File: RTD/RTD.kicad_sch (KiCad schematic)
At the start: 48 parts, among them SW1 SW_SPDT, U1 THVD1420D, U2 STM32F103C8Tx

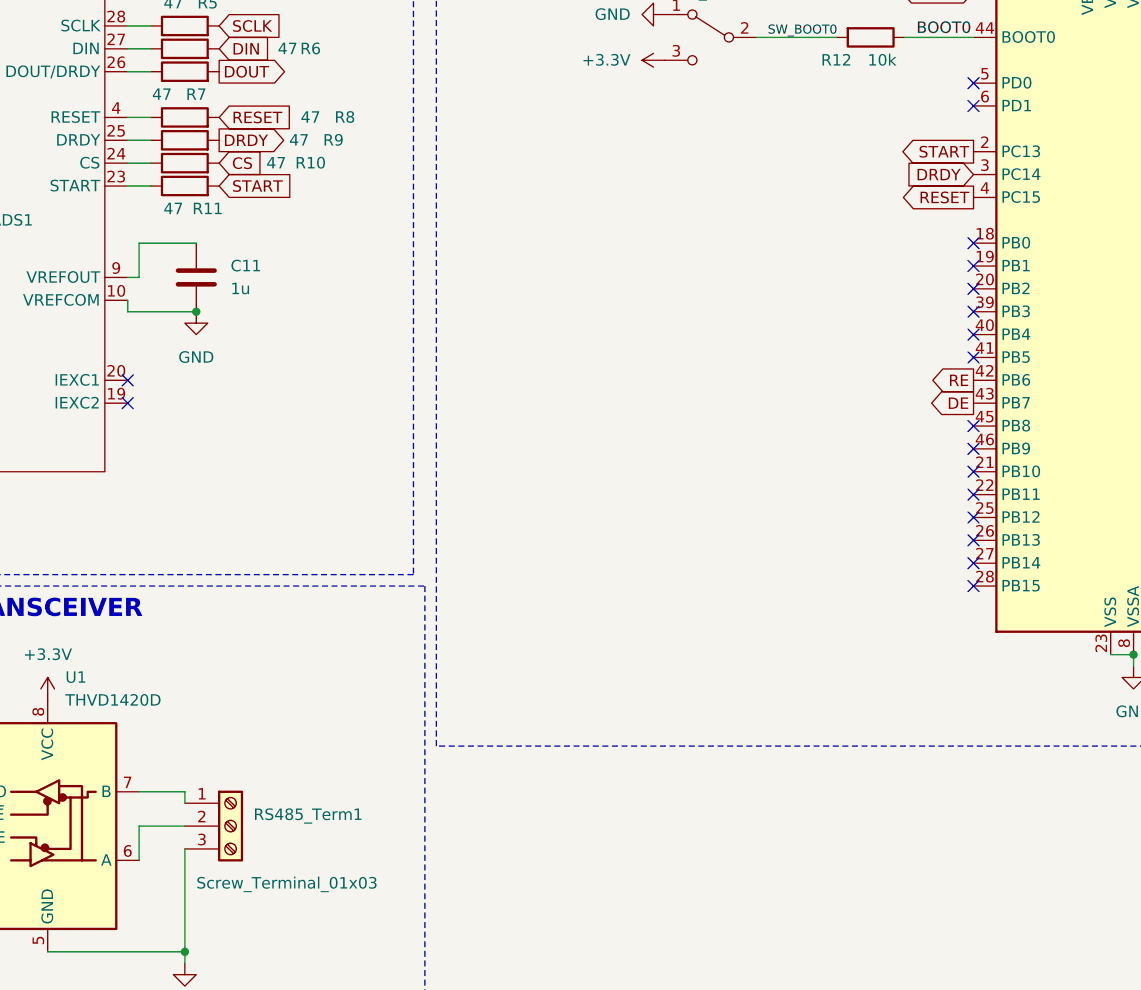
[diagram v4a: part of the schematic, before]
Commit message: feat: adds ADS1248 driver
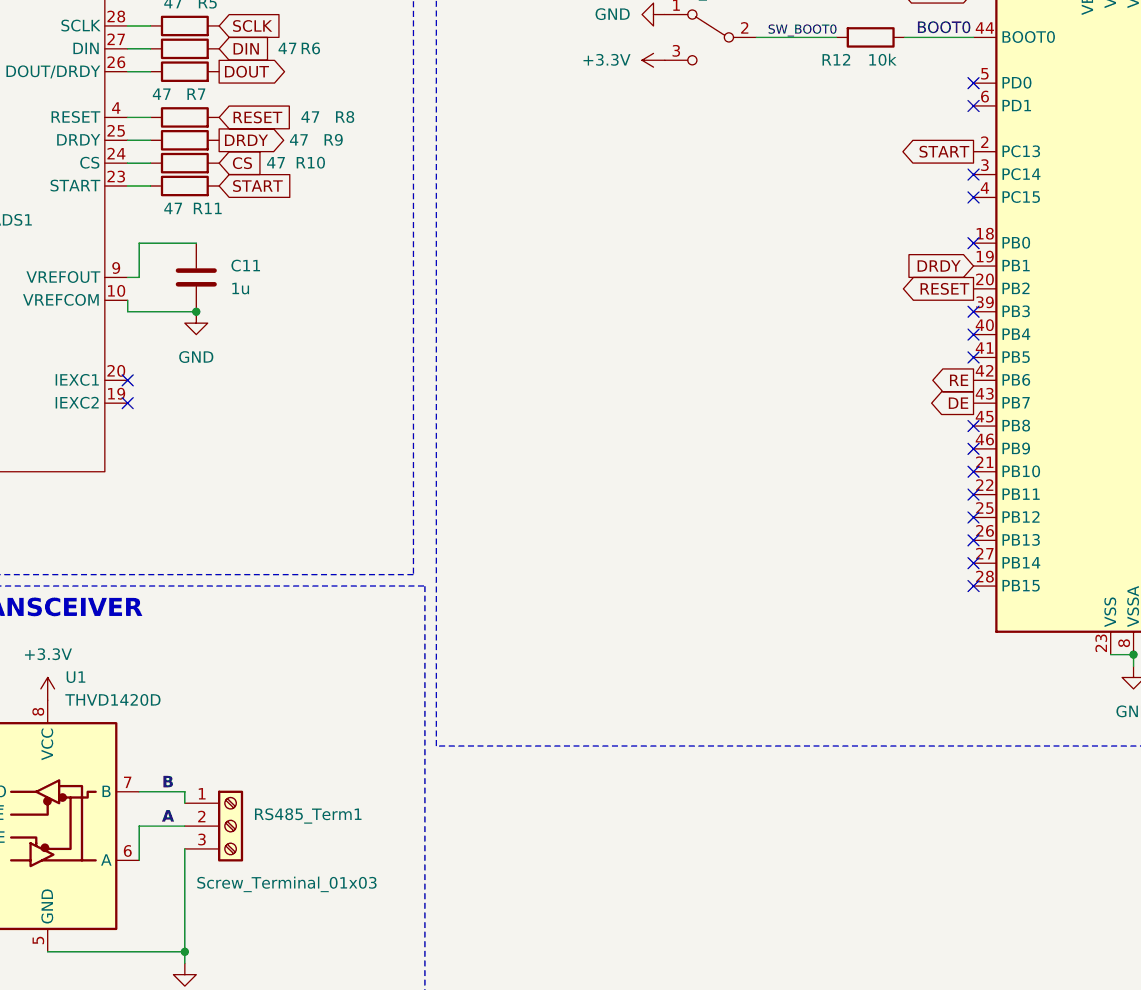
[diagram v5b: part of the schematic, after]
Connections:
- net DRDY: now also U2.19 (PB1); no longer U2.3 (PC14)
- net RESET: now also U2.20 (PB2); no longer U2.4 (PC15)
- net B: now reaches RS485_Term1.1 (Pin_1), U1.7 (B)
- net A: now reaches RS485_Term1.2 (Pin_2), U1.6 (A)
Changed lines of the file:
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@@
   (junction (at 215.9 35.56) (diameter 0) (color 0 0 0 0)
   )
-  (no_connect (at 220.98 74.93))
   (no_connect (at 254 72.39))
+  (no_connect (at 220.98 69.85))
   (no_connect (at 254 80.01))
   (no_connect (at 254 69.85))
   (no_connect (at 90.17 87.63))
   (no_connect (at 220.98 97.79))
-  (no_connect (at 220.98 69.85))
+  (no_connect (at 220.98 62.23))
   (no_connect (at 220.98 102.87))
   (no_connect (at 90.17 69.85))
@@
   (no_connect (at 254 67.31))
   (no_connect (at 220.98 54.61))
-  (no_connect (at 220.98 72.39))
   (no_connect (at 220.98 52.07))
   (no_connect (at 127 87.63))
+  (no_connect (at 220.98 64.77))
   (no_connect (at 220.98 82.55))
   (no_connect (at 90.17 62.23))
@@
     (effects (font (size 2 2) (thickness 0.4) bold) (justify left bottom))
   )
+  (label "A" (at 130.81 134.62 0) (fields_autoplaced)
+    (effects (font (size 1.27 1.27) bold) (justify left bottom))
+  )
   (label "-24V" (at 62.23 140.97 270) (fields_autoplaced)
     (effects (font (size 1.27 1.27)) (justify right bottom))
   )
+  (label "B" (at 130.81 130.81 0) (fields_autoplaced)
+    (effects (font (size 1.27 1.27) bold) (justify left bottom))
+  )
   (label "SW_BOOT0" (at 198.12 46.99 0) (fields_autoplaced)
     (effects (font (size 1 1)) (justify left bottom))
@@
     (effects (font (size 1.27 1.27)) (justify left bottom))
   )
-  (global_label "RESET" (shape output) (at 220.98 64.77 180) (fields_autoplaced)
-    (effects (font (size 1.27 1.27)) (justify right))
-    (property "Intersheetrefs" "${INTERSHEET_REFS}" (at 212.3291 64.77 0)
+  (global_label "RESET" (shape output) (at 220.98 74.93 180) (fields_autoplaced)
+    (effects (font (size 1.27 1.27)) (justify right))
+    (property "Intersheetrefs" "${INTERSHEET_REFS}" (at 212.3291 74.93 0)
       (effects (font (size 1.27 1.27)) (justify right) hide)
     )
@@
     )
   )
-  (global_label "DRDY" (shape input) (at 220.98 62.23 180) (fields_autoplaced)
-    (effects (font (size 1.27 1.27)) (justify right))
-    (property "Intersheetrefs" "${INTERSHEET_REFS}" (at 213.1756 62.23 0)
-      (effects (font (size 1.27 1.27)) (justify right) hide)
-    )
+  (global_label "DRDY" (shape input) (at 220.98 72.39 180) (fields_autoplaced)
+    (effects (font (size 1.27 1.27)) (justify right))
+    (property "Intersheetrefs" "${INTERSHEET_REFS}" (at 213.1756 72.39 0)
+      (effects (font (size 1.27 1.27)) (justify right) hide)
+    )
